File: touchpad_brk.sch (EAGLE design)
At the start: 3 parts

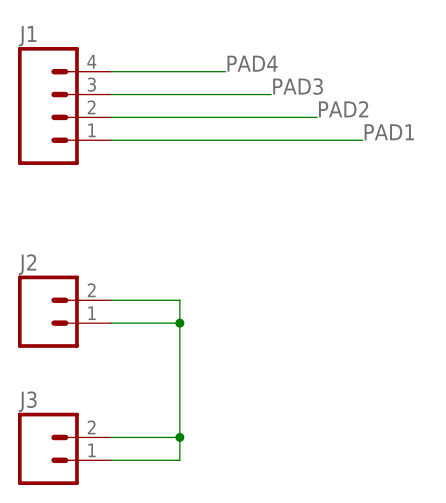
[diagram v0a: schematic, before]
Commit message: Fixes: smaller pads, no grounding pins.
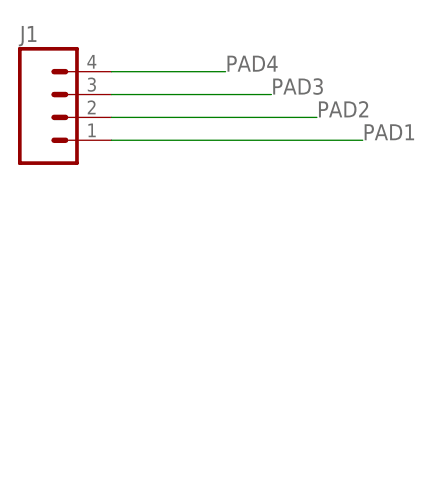
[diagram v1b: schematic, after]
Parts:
- removed J2, J3: (no value), SparkFun-Connectors:M02PTH
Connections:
- removed net GND: J2.1, J2.2, J3.1, J3.2
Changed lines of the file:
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@@
 <?xml version="1.0" encoding="utf-8"?>
 <!DOCTYPE eagle SYSTEM "eagle.dtd">
-<eagle version="8.2.1">
+<eagle version="9.0.1">
 <drawing>
 <settings>
 <setting alwaysvectorfont="no"/>
+<setting keepoldvectorfont="yes"/>
 <setting verticaltext="up"/>
 </settings>
@@
 <part name="FRAME1" library="frames" library_urn="urn:adsk.eagle:library:229" deviceset="A4L-LOC" device=""/>
 <part name="J1" library="SparkFun-Connectors" deviceset="M04" device="PTH"/>
-<part name="J2" library="SparkFun-Connectors" deviceset="M02" device="PTH"/>
-<part name="J3" library="SparkFun-Connectors" deviceset="M02" device="PTH"/>
 </parts>
 <sheets>
@@
 <instance part="FRAME1" gate="G$1" x="0" y="0"/>
 <instance part="J1" gate="G$1" x="55.88" y="109.22"/>
-<instance part="J2" gate="G$1" x="53.34" y="86.36"/>
-<instance part="J3" gate="G$1" x="53.34" y="71.12"/>
 </instances>
 <busses>
@@
 <wire x1="60.96" y1="106.68" x2="88.9" y2="106.68" width="0.1524" layer="91"/>
 <label x="88.9" y="106.68" size="1.778" layer="95"/>
-</segment>
-</net>
-<net name="GND" class="0">
-<segment>
-<pinref part="J2" gate="G$1" pin="2"/>
-<wire x1="60.96" y1="88.9" x2="68.58" y2="88.9" width="0.1524" layer="91"/>
-<pinref part="J2" gate="G$1" pin="1"/>
-<wire x1="60.96" y1="86.36" x2="68.58" y2="86.36" width="0.1524" layer="91"/>
-<wire x1="68.58" y1="88.9" x2="68.58" y2="86.36" width="0.1524" layer="91"/>
-<pinref part="J3" gate="G$1" pin="2"/>
-<wire x1="60.96" y1="73.66" x2="68.58" y2="73.66" width="0.1524" layer="91"/>
-<wire x1="68.58" y1="86.36" x2="68.58" y2="73.66" width="0.1524" layer="91"/>
-<junction x="68.58" y="86.36"/>
-<pinref part="J3" gate="G$1" pin="1"/>
-<wire x1="60.96" y1="71.12" x2="68.58" y2="71.12" width="0.1524" layer="91"/>
-<wire x1="68.58" y1="73.66" x2="68.58" y2="71.12" width="0.1524" layer="91"/>
-<junction x="68.58" y="73.66"/>
 </segment>
 </net>
@@
 <compatibility>
 <note version="8.2" severity="warning">
-Since Version 8.2, Eagle supports online libraries. The ids
+Since Version 8.2, EAGLE supports online libraries. The ids
 of those online libraries will not be understood (or retained)
 with this version.
